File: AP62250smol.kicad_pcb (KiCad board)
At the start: 2 copper layers, 19 x 11.5 mm, 12 parts, among them J1 Heatsink Pads, J2 Connector Pads, U1 AP62250Z6

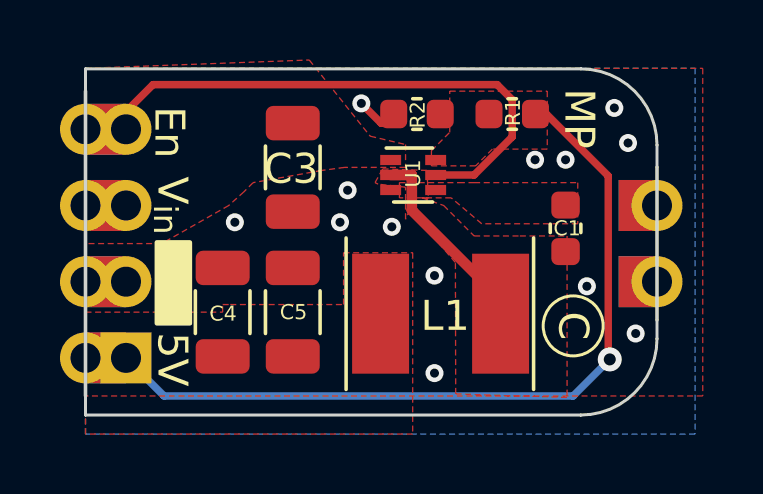
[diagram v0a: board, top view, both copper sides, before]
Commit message: Updated IC footprint to allow 0.2mm spacing between pads. This allows for solder mask between pads if ordering green solder mask from JLCPCB
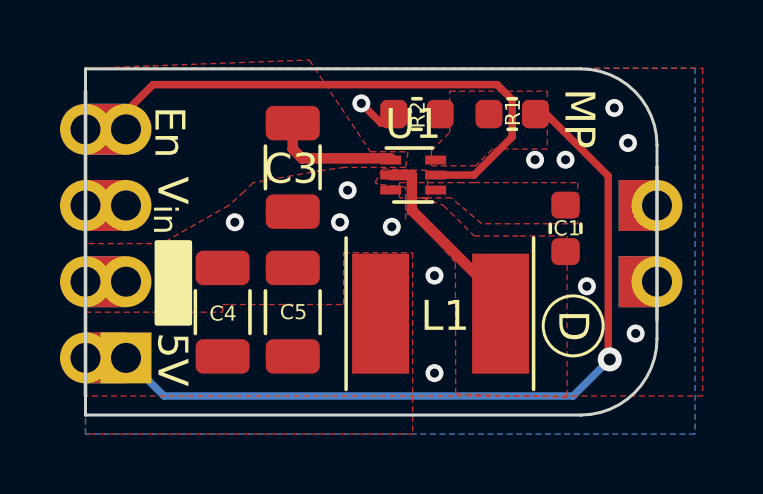
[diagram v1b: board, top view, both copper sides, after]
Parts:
- MISC1: value C -> D
- U1: footprint Package_TO_SOT_SMD:SOT-563 -> MikeFootprintLib:SOT-563_wider_clearance
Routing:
- net V_{IN}: track 0.00 -> 4.26 mm
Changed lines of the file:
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@@
       (effects (font (size 1 1) (thickness 0.15)))
     )
-    (fp_text value "C" (at 0 0 -90 unlocked) (layer "F.SilkS")
+    (fp_text value "D" (at 0 0 -90 unlocked) (layer "F.SilkS")
       (effects (font (size 1 1) (thickness 0.2)))
     )
@@
     )
   )
-  (footprint "Package_TO_SOT_SMD:SOT-563" (layer "F.Cu")
+  (footprint "MikeFootprintLib:SOT-563_wider_clearance" (layer "F.Cu")
     (at 135.382 86.614)
     (descr "SOT563")
@@
     (property "Sheetfile" "AP62250smol.kicad_sch")
     (property "Sheetname" "")
-    (clearance 0.125)
     (attr smd)
-    (fp_text reference "U1" (at 0 -0.0508 270) (layer "F.SilkS")
-      (effects (font (size 0.5 0.5) (thickness 0.125)))
-    )
-    (fp_text value "AP62250Z6" (at 4.7752 1.778) (layer "F.Fab")
+    (fp_text reference "U1" (at 0 -1.7) (layer "F.SilkS")
+      (effects (font (size 1 1) (thickness 0.15)))
+    )
+    (fp_text value "AP62250Z6" (at 0 1.75) (layer "F.Fab")
       (effects (font (size 1 1) (thickness 0.15)))
     )
@@
     (fp_line (start 0.65 0.9) (end -0.65 0.9) (layer "F.SilkS") (width 0.12))
     (fp_line (start -0.9 -0.9) (end 0.65 -0.9) (layer "F.SilkS") (width 0.12))
+    (fp_line (start 1.35 1.1) (end 1.35 -1.1) (layer "F.CrtYd") (width 0.05))
+    (fp_line (start -1.35 -1.1) (end 1.35 -1.1) (layer "F.CrtYd") (width 0.05))
     (fp_line (start 1.35 1.1) (end -1.35 1.1) (layer "F.CrtYd") (width 0.05))
-    (fp_line (start 1.35 1.1) (end 1.35 -1.1) (layer "F.CrtYd") (width 0.05))
     (fp_line (start -1.35 -1.1) (end -1.35 1.1) (layer "F.CrtYd") (width 0.05))
-    (fp_line (start -1.35 -1.1) (end 1.35 -1.1) (layer "F.CrtYd") (width 0.05))
+    (fp_line (start -0.65 -0.5) (end -0.65 0.85) (layer "F.Fab") (width 0.1))
+    (fp_line (start -0.65 -0.5) (end -0.3 -0.85) (layer "F.Fab") (width 0.1))
     (fp_line (start 0.65 0.85) (end 0.65 -0.85) (layer "F.Fab") (width 0.1))
     (fp_line (start 0.65 -0.85) (end -0.3 -0.85) (layer "F.Fab") (width 0.1))
     (fp_line (start -0.65 0.85) (end 0.65 0.85) (layer "F.Fab") (width 0.1))
-    (fp_line (start -0.65 -0.5) (end -0.3 -0.85) (layer "F.Fab") (width 0.1))
-    (fp_line (start -0.65 -0.5) (end -0.65 0.85) (layer "F.Fab") (width 0.1))
-    (pad "1" smd rect locked (at -0.75 -0.5) (size 0.7 0.34) (layers "F.Cu" "F.Paste" "F.Mask")
+    (pad "1" smd rect (at -0.75 -0.5) (size 0.7 0.3) (layers "F.Cu" "F.Paste" "F.Mask")
       (net 1 "V_{IN}") (pinfunction "VIN") (pintype "power_in"))
-    (pad "2" smd rect locked (at -0.75 0) (size 0.7 0.34) (layers "F.Cu" "F.Paste" "F.Mask")
+    (pad "2" smd rect (at -0.75 0) (size 0.7 0.3) (layers "F.Cu" "F.Paste" "F.Mask")
       (net 4 "Net-(C1-Pad1)") (pinfunction "SW") (pintype "output"))
-    (pad "3" smd rect locked (at -0.75 0.5) (size 0.7 0.34) (layers "F.Cu" "F.Paste" "F.Mask")
+    (pad "3" smd rect (at -0.75 0.5) (size 0.7 0.3) (layers "F.Cu" "F.Paste" "F.Mask")
       (net 2 "GND") (pinfunction "GND") (pintype "power_in"))
-    (pad "4" smd rect locked (at 0.75 0.5) (size 0.7 0.34) (layers "F.Cu" "F.Paste" "F.Mask")
+    (pad "4" smd rect (at 0.75 0.5) (size 0.7 0.3) (layers "F.Cu" "F.Paste" "F.Mask")
       (net 5 "Net-(C1-Pad2)") (pinfunction "BST") (pintype "passive"))
-    (pad "5" smd rect locked (at 0.75 0) (size 0.7 0.34) (layers "F.Cu" "F.Paste" "F.Mask")
+    (pad "5" smd rect (at 0.75 0) (size 0.7 0.3) (layers "F.Cu" "F.Paste" "F.Mask")
       (net 6 "En") (pinfunction "EN") (pintype "input"))
-    (pad "6" smd rect locked (at 0.75 -0.5) (size 0.7 0.34) (layers "F.Cu" "F.Paste" "F.Mask")
+    (pad "6" smd rect (at 0.75 -0.5) (size 0.7 0.3) (layers "F.Cu" "F.Paste" "F.Mask")
       (net 3 "Net-(R1-Pad2)") (pinfunction "FB") (pintype "input"))
     (model "${KICAD6_3DMODEL_DIR}/Package_TO_SOT_SMD.3dshapes/SOT-563.wrl"
@@
     (effects (font (size 1 1) (thickness 0.15)))
   )
+  (segment (start 131.3688 84.885) (end 131.3688 85.7488) (width 0.3556) (layer "F.Cu") (net 1))
+  (segment (start 131.67888 86.05888) (end 134.632 86.05888) (width 0.3556) (layer "F.Cu") (net 1))
+  (segment (start 131.3688 85.7488) (end 131.67888 86.05888) (width 0.3556) (layer "F.Cu") (net 1))
   (segment (start 133.6548 84.2264) (end 134.3152 84.8868) (width 0.25) (layer "F.Cu") (net 2))
   (segment (start 134.3152 84.8868) (end 134.5562 84.8868) (width 0.25) (layer "F.Cu") (net 2))
@@
   )
   (zone (net 2) (net_name "GND") (layer "F.Cu") (hatch edge 0.508)
-    (connect_pads yes (clearance 0.254))
+    (connect_pads (clearance 0.254))
     (min_thickness 0.254) (filled_areas_thickness no)
     (fill yes (thermal_gap 0.33) (thermal_bridge_width 0.508))
@@
   (zone (net 1) (net_name "V_{IN}") (layer "F.Cu") (hatch edge 0.508)
     (priority 12)
-    (connect_pads yes (clearance 0.254))
+    (connect_pads (clearance 0.254))
     (min_thickness 0.254) (filled_areas_thickness no)
     (fill yes (thermal_gap 0.33) (thermal_bridge_width 0.508))
     (polygon
       (pts
-        (xy 133.950927 85.320459)
-        (xy 135.128 85.598)
+        (xy 133.96 85.84)
+        (xy 135.21 85.84)
         (xy 135.128 86.36)
         (xy 133.096 86.36)

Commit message: a
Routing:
- net V_{IN}: track 4.26 -> 5.73 mm
- net GND: track 1.17 -> 2.20 mm
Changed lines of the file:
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@@
   )
   (segment (start 131.3688 84.885) (end 131.3688 85.7488) (width 0.3556) (layer "F.Cu") (net 1))
-  (segment (start 131.67888 86.05888) (end 134.632 86.05888) (width 0.3556) (layer "F.Cu") (net 1))
+  (segment (start 134.632 86.114) (end 131.484 86.114) (width 0.25) (layer "F.Cu") (net 1))
+  (segment (start 131.484 86.114) (end 131.3688 85.9988) (width 0.25) (layer "F.Cu") (net 1))
   (segment (start 131.3688 85.7488) (end 131.67888 86.05888) (width 0.3556) (layer "F.Cu") (net 1))
+  (segment (start 131.3688 85.9988) (end 131.3688 84.885) (width 0.25) (layer "F.Cu") (net 1))
   (segment (start 133.6548 84.2264) (end 134.3152 84.8868) (width 0.25) (layer "F.Cu") (net 2))
+  (segment (start 133.216911 87.141311) (end 134.21 87.141311) (width 0.3556) (layer "F.Cu") (net 2))
+  (segment (start 133.1976 87.122) (end 133.216911 87.141311) (width 0.3556) (layer "F.Cu") (net 2))
   (segment (start 134.3152 84.8868) (end 134.5562 84.8868) (width 0.25) (layer "F.Cu") (net 2))
   (via (at 140.462 86.106) (size 0.6) (drill 0.3) (layers "F.Cu" "B.Cu") (free) (net 2))
@@
   (via (at 136.0932 89.9668) (size 0.6) (drill 0.3) (layers "F.Cu" "B.Cu") (free) (net 2))
   (via (at 134.6708 88.3412) (size 0.6) (drill 0.3) (layers "F.Cu" "B.Cu") (free) (net 2))
-  (segment (start 135.3376 86.614) (end 135.3376 87.7888) (width 0.3556) (layer "F.Cu") (net 4))
-  (segment (start 134.632 86.614) (end 135.3376 86.614) (width 0.3556) (layer "F.Cu") (net 4))
+  (segment (start 134.632 86.614) (end 135.385022 86.614) (width 0.25) (layer "F.Cu") (net 4))
+  (segment (start 135.457489 86.686467) (end 135.457489 87.668911) (width 0.25) (layer "F.Cu") (net 4))
+  (segment (start 135.385022 86.614) (end 135.457489 86.686467) (width 0.25) (layer "F.Cu") (net 4))
+  (segment (start 135.457489 87.668911) (end 135.3376 87.7888) (width 0.25) (layer "F.Cu") (net 4))
   (segment (start 135.3376 87.7888) (end 138.2964 90.7476) (width 0.3556) (layer "F.Cu") (net 4))
   (segment (start 137.414 86.614) (end 136.132 86.614) (width 0.25) (layer "F.Cu") (net 6))
